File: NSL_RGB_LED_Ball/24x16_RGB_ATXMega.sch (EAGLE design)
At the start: 107 parts, among them IC2 TLC5947XLP, IC3 TLC5947XLP, IC4 TLC5947XLP, IC5 MCP73123, IC6 BLUETOOTH-RN41", IC7 MMA7455L, IC8 OPA344, Q1 BSH201, X1 NX3225GA XC1972CT-ND

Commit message: 
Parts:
- C15: value 1uF -> 10uF
- R5: value 1.5K -> 1K
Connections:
- net BUTTON: now also IC1.PC3/OC0D/TXD0; no longer IC1.SS/PD4
- net RX: now also IC1.PC6/MISO/RXD1; no longer IC1.PC2/OC0C/RXD0
- net TX: now also IC1.PC7/SCK/TXD1/CLKO/EVO; no longer IC1.PC3/OC0D/TXD0
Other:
- note added: "http://www.batteryspace.com/High-Power-LiNiMnCo-26650-Rechargeable-Cell-3.6V-3600mAh-13Wh-18A-Rate.aspx"
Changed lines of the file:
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@@
 <part name="GND6" library="SparkFun" deviceset="GND" device=""/>
 <part name="GND7" library="SparkFun" deviceset="GND" device=""/>
-<part name="R5" library="slice_noshift" deviceset="RESISTOR" device="0805" value="1.5K">
+<part name="R5" library="slice_noshift" deviceset="RESISTOR" device="0805" value="1K">
 <attribute name="MF" value=""/>
 <attribute name="MPN" value=""/>
@@
 </part>
 <part name="GND11" library="SparkFun" deviceset="GND" device=""/>
-<part name="C15" library="24x16_RGB" deviceset="CAP" device="0805" value="1uF">
+<part name="C15" library="24x16_RGB" deviceset="CAP" device="0805" value="10uF">
 <attribute name="MF" value=""/>
 <attribute name="MPN" value="08055D105KAT2A"/>
@@
 <net name="TX" class="0">
 <segment>
-<pinref part="IC1" gate="G$1" pin="PC3/OC0D/TXD0"/>
-<wire x1="-55.88" y1="-62.23" x2="-38.1" y2="-62.23" width="0.1524" layer="91"/>
-<label x="-54.61" y="-62.23" size="1.778" layer="95"/>
+<wire x1="-55.88" y1="-72.39" x2="-38.1" y2="-72.39" width="0.1524" layer="91"/>
+<pinref part="IC1" gate="G$1" pin="PC7/SCK/TXD1/CLKO/EVO"/>
 </segment>
 </net>
 <net name="RX" class="0">
 <segment>
-<pinref part="IC1" gate="G$1" pin="PC2/OC0C/RXD0"/>
-<wire x1="-55.88" y1="-59.69" x2="-38.1" y2="-59.69" width="0.1524" layer="91"/>
-<label x="-54.61" y="-59.69" size="1.778" layer="95"/>
+<wire x1="-55.88" y1="-69.85" x2="-38.1" y2="-69.85" width="0.1524" layer="91"/>
+<pinref part="IC1" gate="G$1" pin="PC6/MISO/RXD1"/>
 </segment>
 </net>
@@
 <net name="BUTTON" class="0">
 <segment>
-<wire x1="22.86" y1="-26.67" x2="50.8" y2="-26.67" width="0.1524" layer="91"/>
-<label x="44.45" y="-26.67" size="1.778" layer="95"/>
-<pinref part="IC1" gate="G$1" pin="SS/PD4"/>
+<wire x1="-60.96" y1="-62.23" x2="-38.1" y2="-62.23" width="0.1524" layer="91"/>
+<pinref part="IC1" gate="G$1" pin="PC3/OC0D/TXD0"/>
 </segment>
 </net>
@@
 <plain>
 <text x="-53.34" y="-40.64" size="1.778" layer="91">http://www.batteryspace.com/lifepo426650cell32v3300mah19.8arate10whunapproved.aspx</text>
+<text x="-60.96" y="-45.72" size="1.778" layer="91">http://www.batteryspace.com/High-Power-LiNiMnCo-26650-Rechargeable-Cell-3.6V-3600mAh-13Wh-18A-Rate.aspx</text>
 </plain>
 <instances>

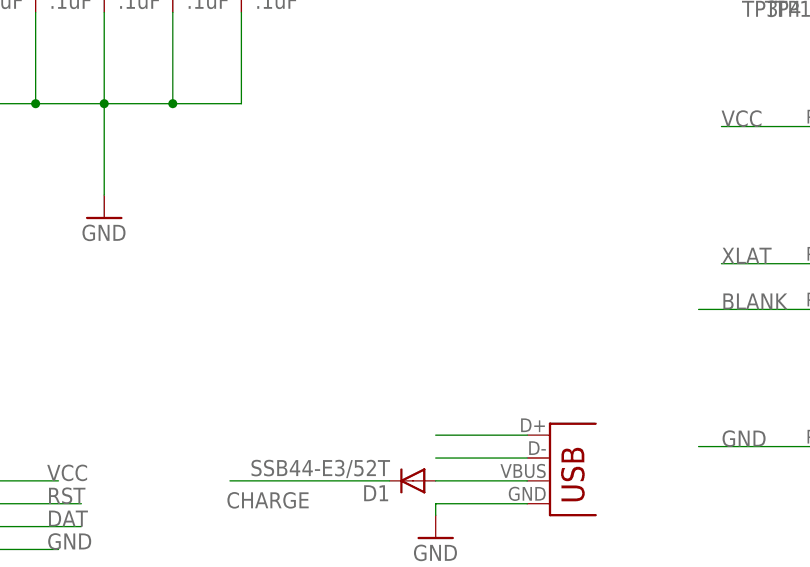
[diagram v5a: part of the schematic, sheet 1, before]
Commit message: 
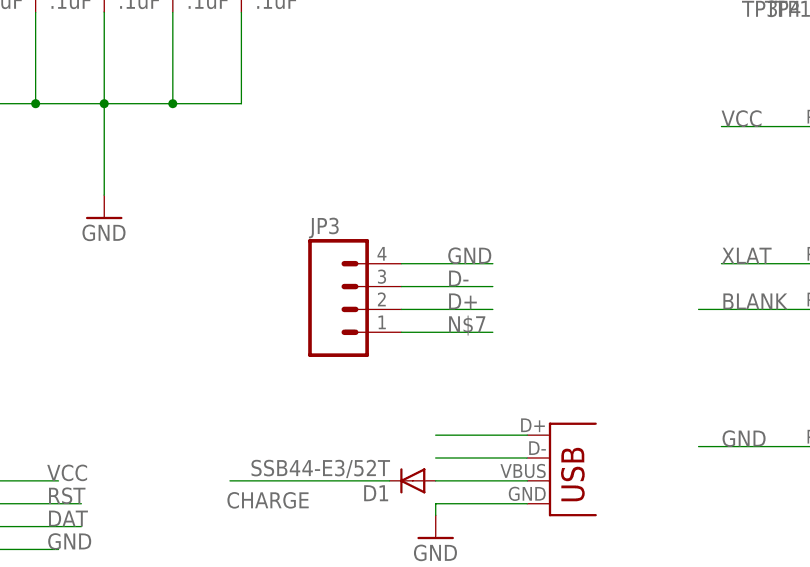
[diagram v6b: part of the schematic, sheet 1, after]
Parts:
- added JP3: (no value), SparkFun-Connectors:M041.27MM
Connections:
- net D+: now also JP3.2
- net D-: now also JP3.3
- net GND: now also JP3.4
- net N$7: now also JP3.1
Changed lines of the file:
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@@
 <part name="GND13" library="SparkFun" deviceset="GND" device=""/>
 <part name="D1" library="diode" deviceset="DIODE-" device="DO214AA" value="SSB44-E3/52T"/>
+<part name="JP3" library="SparkFun-Connectors" deviceset="M04" device="1.27MM"/>
 </parts>
 <sheets>
@@
 <instance part="GND12" gate="1" x="-21.59" y="2.54"/>
 <instance part="D1" gate="G$1" x="-24.13" y="8.89" rot="R180"/>
+<instance part="JP3" gate="G$1" x="-30.48" y="27.94"/>
 </instances>
 <busses>
@@
 <wire x1="-21.59" y1="6.35" x2="-21.59" y2="5.08" width="0.1524" layer="91"/>
 <pinref part="JP2" gate="G$1" pin="GND"/>
+</segment>
+<segment>
+<wire x1="-15.24" y1="33.02" x2="-25.4" y2="33.02" width="0.1524" layer="91"/>
+<pinref part="JP3" gate="G$1" pin="4"/>
+<label x="-20.32" y="33.02" size="1.778" layer="95"/>
 </segment>
 </net>
@@
 <pinref part="JP2" gate="G$1" pin="D-"/>
 </segment>
+<segment>
+<wire x1="-25.4" y1="30.48" x2="-15.24" y2="30.48" width="0.1524" layer="91"/>
+<label x="-20.32" y="30.48" size="1.778" layer="95"/>
+<pinref part="JP3" gate="G$1" pin="3"/>
+</segment>
 </net>
 <net name="D+" class="0">
@@
 <wire x1="-21.59" y1="13.97" x2="-11.43" y2="13.97" width="0.1524" layer="91"/>
 <pinref part="JP2" gate="G$1" pin="D+"/>
+</segment>
+<segment>
+<wire x1="-25.4" y1="27.94" x2="-15.24" y2="27.94" width="0.1524" layer="91"/>
+<pinref part="JP3" gate="G$1" pin="2"/>
+<label x="-20.32" y="27.94" size="1.778" layer="95"/>
 </segment>
 </net>
@@
 <wire x1="-11.43" y1="8.89" x2="-21.59" y2="8.89" width="0.1524" layer="91"/>
 </segment>
-</net>
+<segment>
+<wire x1="-15.24" y1="25.4" x2="-25.4" y2="25.4" width="0.1524" layer="91"/>
+<pinref part="JP3" gate="G$1" pin="1"/>
+<label x="-20.32" y="25.4" size="1.778" layer="95"/>
+</segment>
+</net>
